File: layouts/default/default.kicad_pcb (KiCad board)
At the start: 2 copper layers, 36 x 36 mm, 109 parts

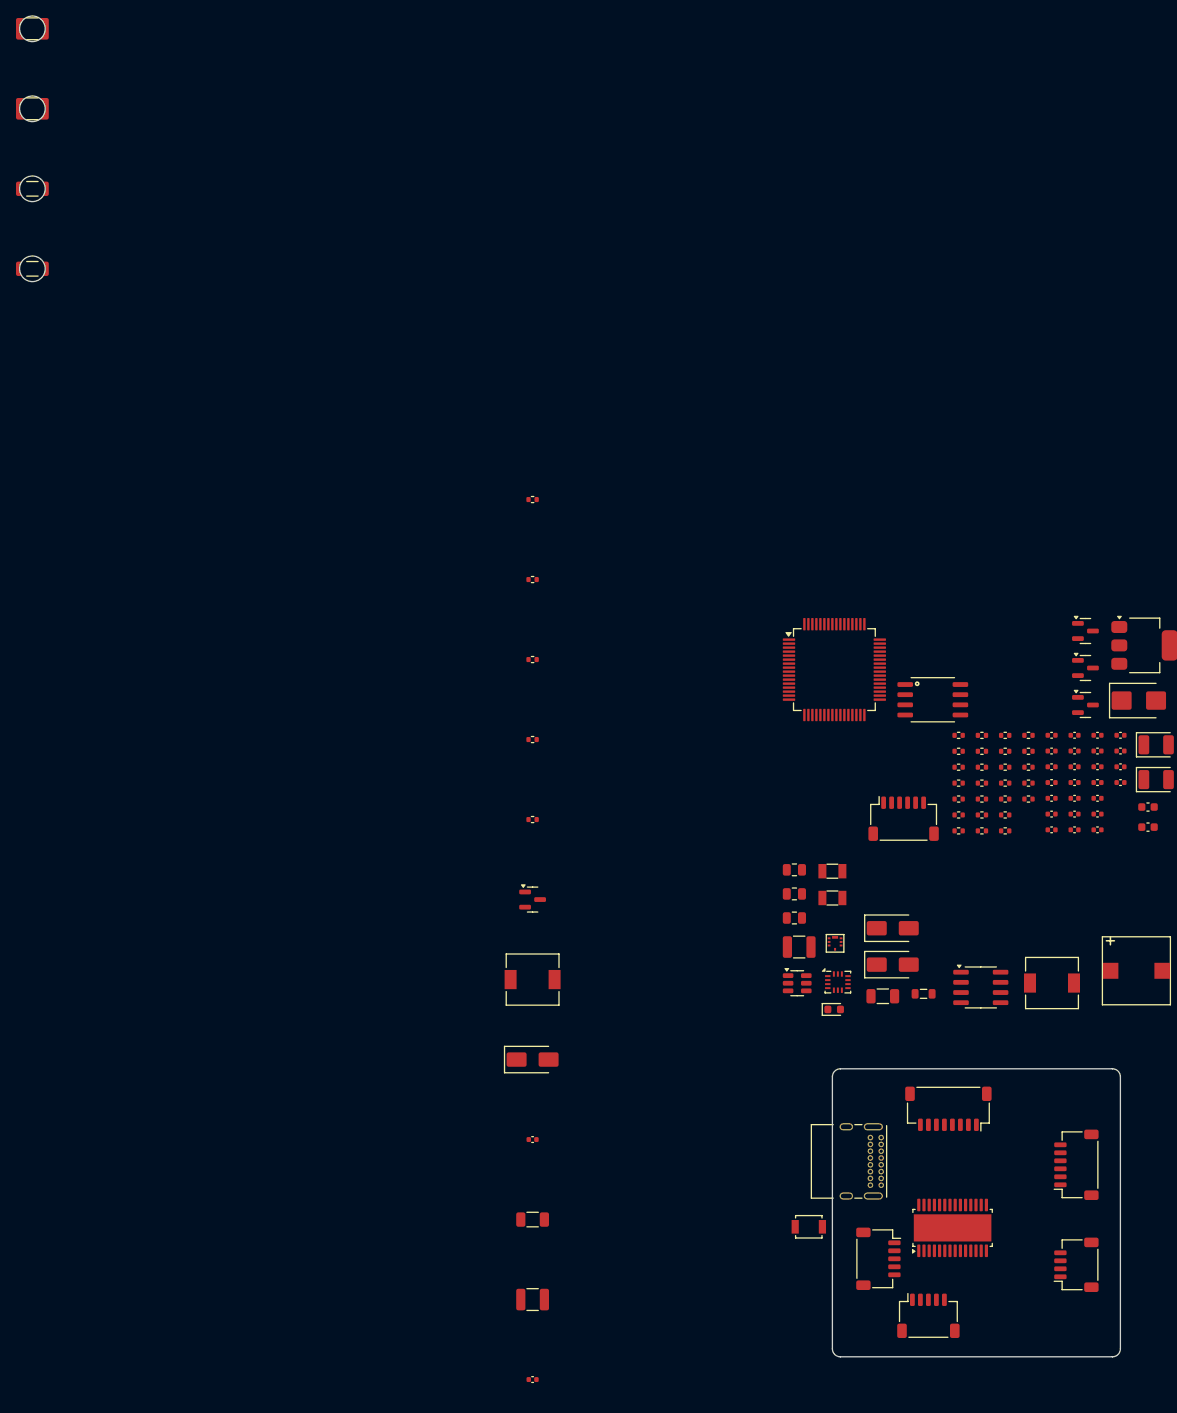
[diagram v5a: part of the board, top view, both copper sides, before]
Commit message: Resize board to 37x37mm with 30x30mm mounting pattern
Match Brave F7 reference dimensions. Board outline expanded from 36mm to
37mm in KiCad PCB. Mounting holes updated to 30x30mm pattern (3.5mm edge
offset). Specs, weight budget, and comments updated accordingly.

Co-Authored-By: Claude Opus 4.6 <noreply@anthropic.com>
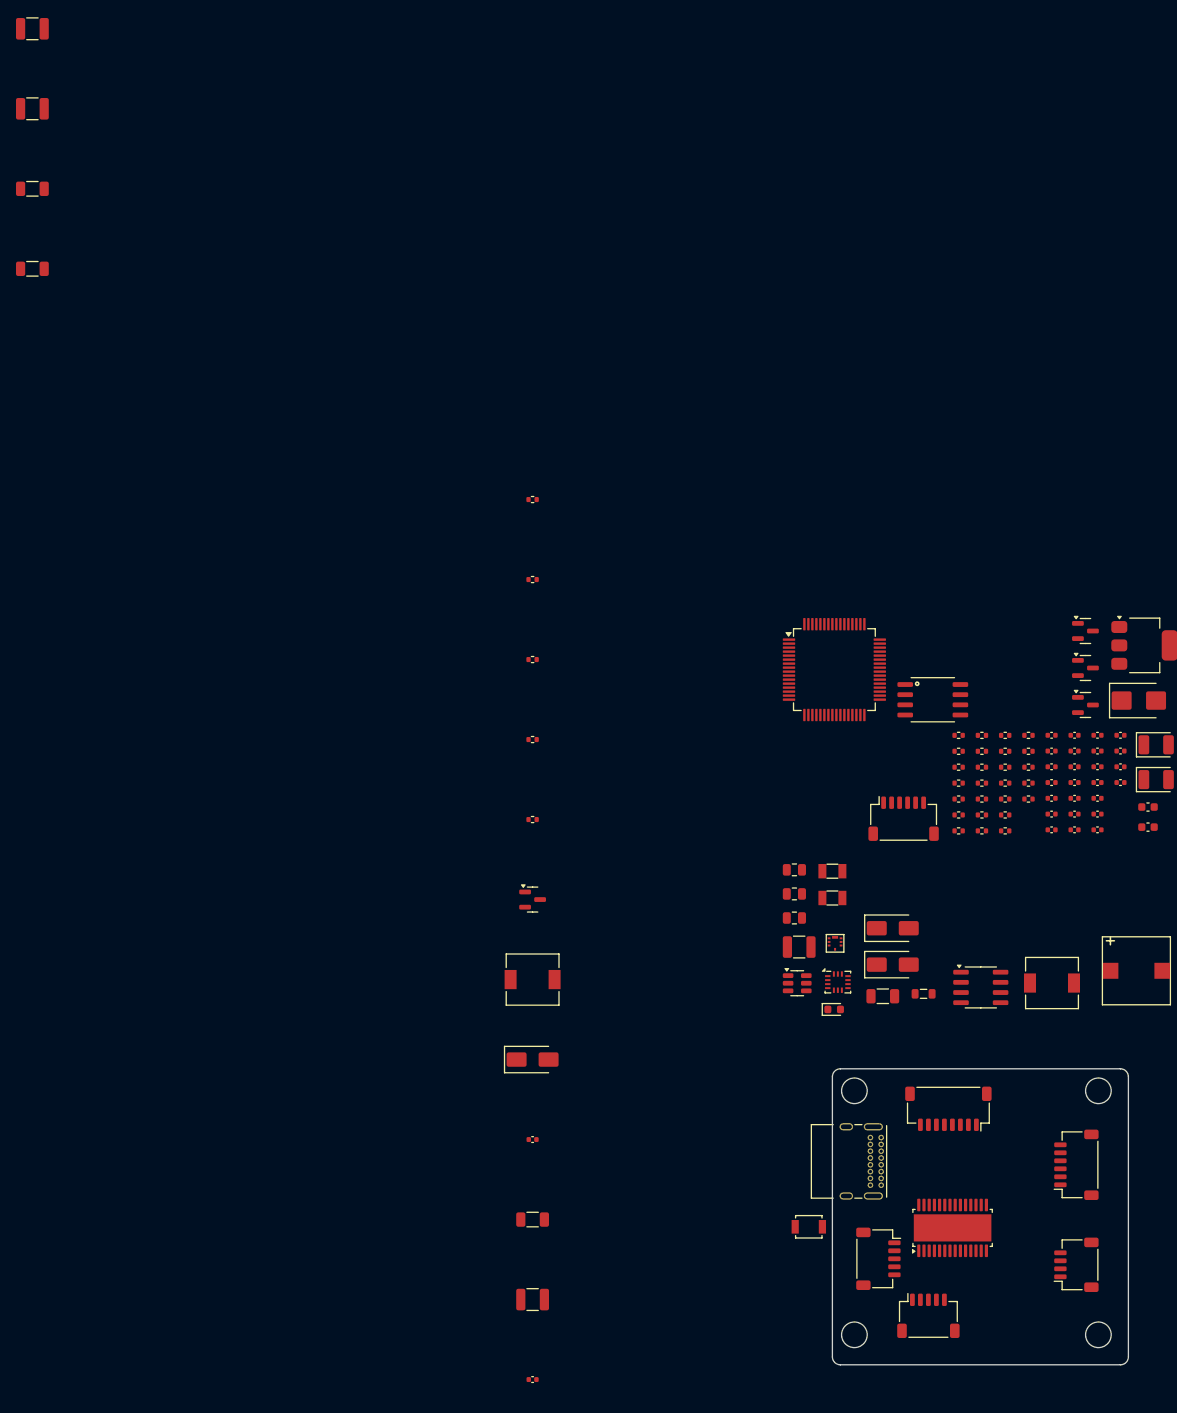
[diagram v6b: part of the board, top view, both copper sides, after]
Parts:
- moved H4 210.7 mm to (133.2, 133.2)
- moved H3 181.2 mm to (133.2, 102.8)
- moved H2 176.3 mm to (102.8, 133.2)
- moved H1 145.3 mm to (102.8, 102.8)
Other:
- board size 36 x 36 mm -> 37 x 37 mm

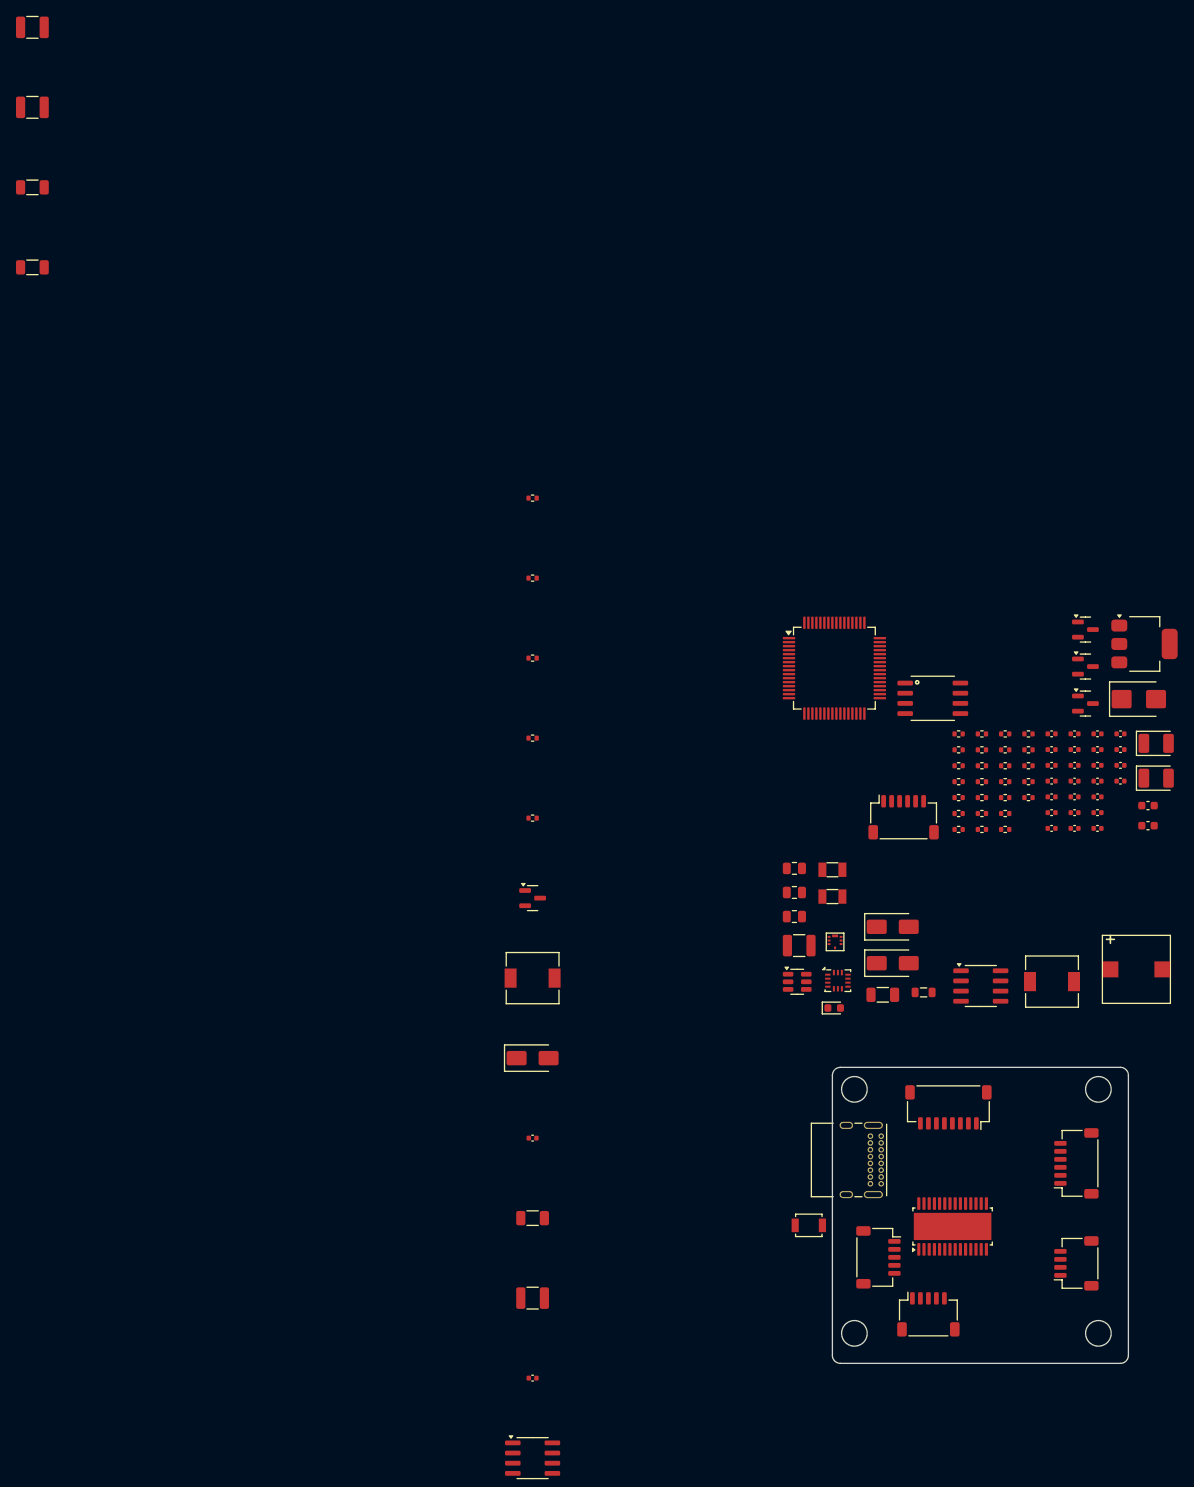
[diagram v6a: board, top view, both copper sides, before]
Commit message: Unhide all reference designators on PCB silkscreen
Make all 95 component reference designators (Y2, U3, R14, etc.) visible
on F.SilkS layer for easier identification during layout and review.

Co-Authored-By: Claude Opus 4.6 <noreply@anthropic.com>
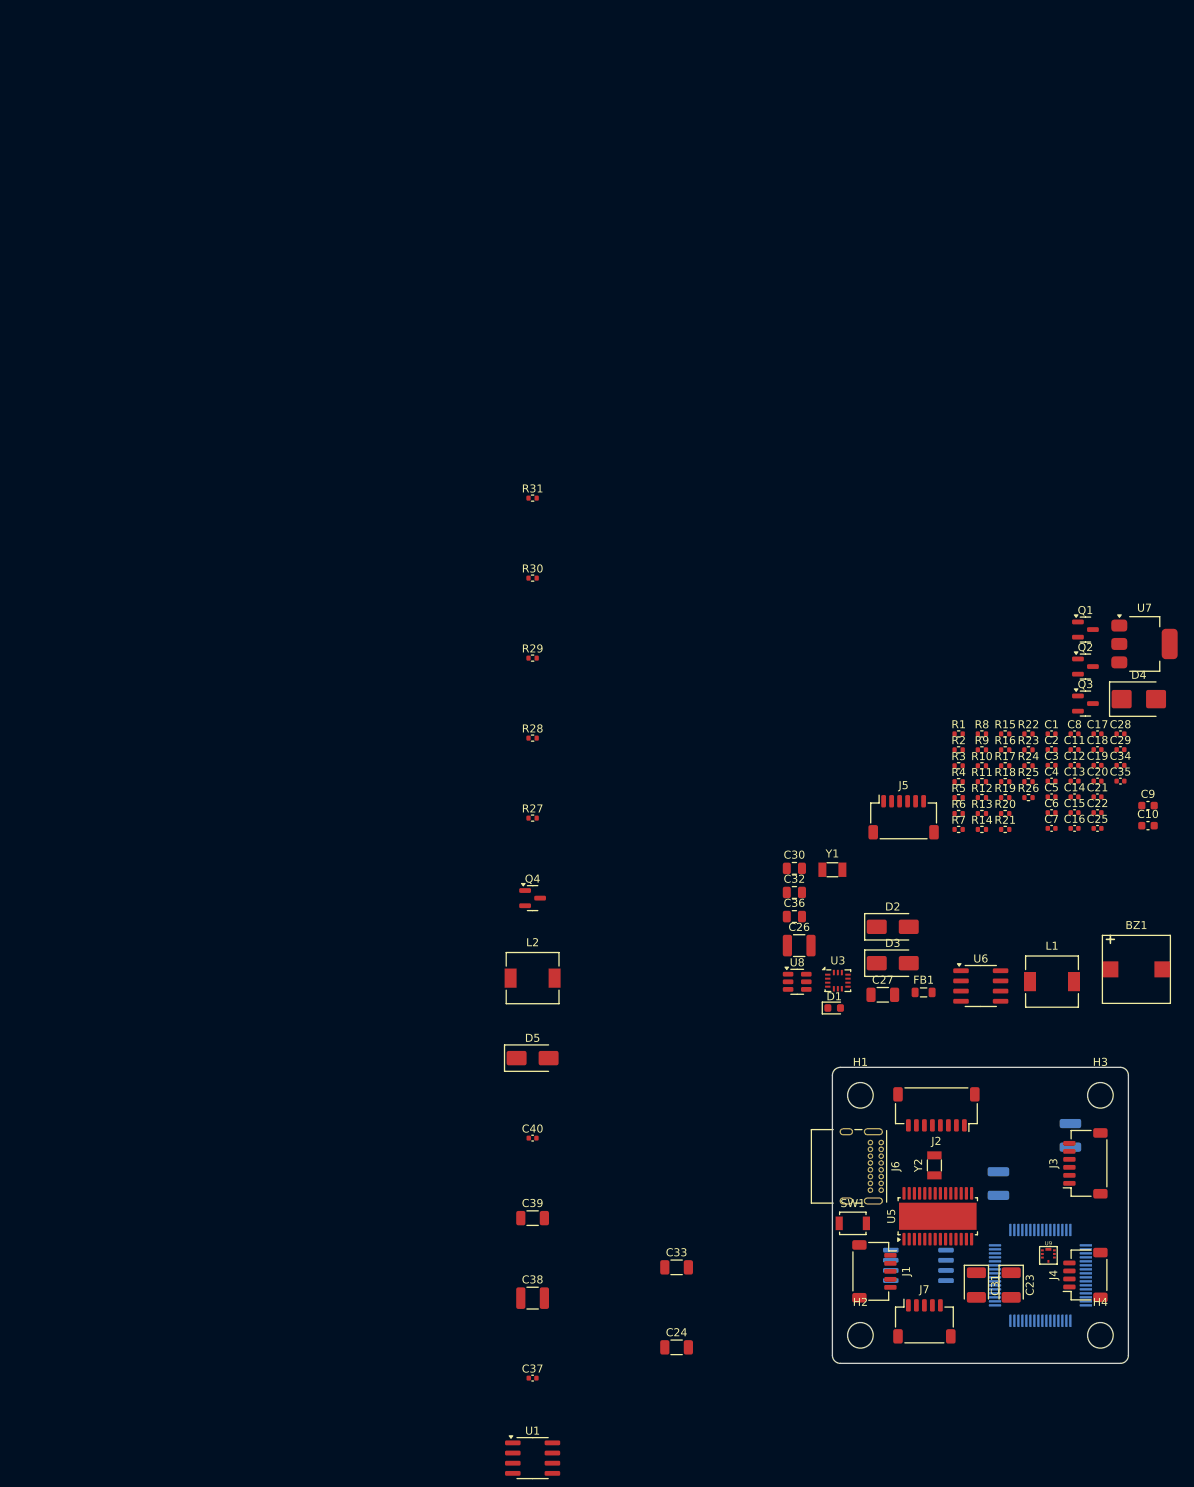
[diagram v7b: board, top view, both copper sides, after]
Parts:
- C41, C42, U10, U4: moved to B.Cu
- moved C42 188.3 mm to (120.8, 114.5), turned to -90 degrees
- moved C41 182.6 mm to (129.8, 108.5), turned to 90 degrees
- moved C24 157.2 mm to (80.5, 135.0)
- moved C33 157.2 mm to (80.5, 125.0)
- moved U4 80.1 mm to (126.0, 126.0)
- moved U10 70.9 mm to (110.8, 124.8)
- moved C23 70.1 mm to (122.3, 127.2), turned to -90 degrees
- moved C31 67.2 mm to (118.0, 127.2), turned to -90 degrees
- moved U9 47.4 mm to (127.0, 123.5)
- moved Y2 35.9 mm to (112.8, 112.2), turned to 90 degrees
- moved SW1 5.51 mm to (102.5, 119.5)
- moved U5 2.25 mm to (113.2, 118.6)
- moved J4 1.84 mm to (131.6, 126.0)
- moved J1 1.82 mm to (105.2, 125.5)
- moved J2 1.52 mm to (113.0, 105.2)
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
